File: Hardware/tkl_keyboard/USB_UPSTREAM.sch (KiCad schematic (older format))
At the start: 20 parts, among them J1 USB_C_Receptacle_USB2.0, U1 TCR2EF33, U2 SRV05-4

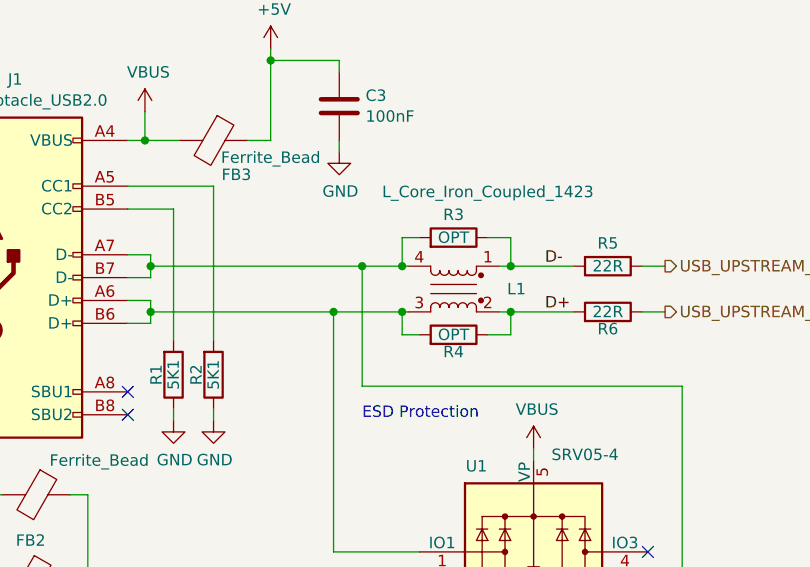
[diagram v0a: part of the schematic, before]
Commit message: Rows and columns routed to controller. Extended top board edge to fit OLED. Removed optional resistors around CMC.
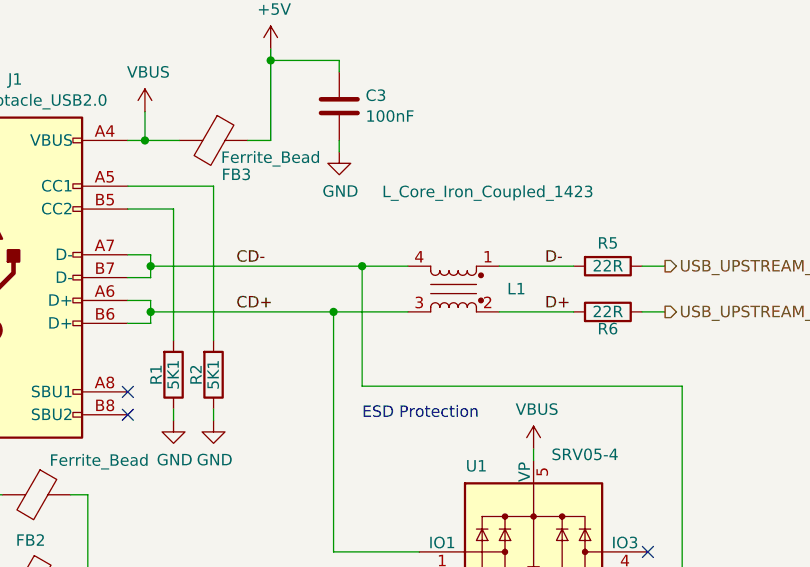
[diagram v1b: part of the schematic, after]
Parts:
- removed R5, R6: OPT, resistor_smd:R_0603_1608Metric, symbol Device:R
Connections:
- net CD+: now reaches J1.A6 (D+), J1.B6 (D+), L1.3, U2.1 (IO1)
- net CD-: now reaches J1.A7 (D-), J1.B7 (D-), L1.4, U2.6 (IO4)
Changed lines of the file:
@@
 	-1   0    0    -1
 $EndComp
-Wire Wire Line
-	5675 3775 5725 3775
-$Comp
-L Device:R R6
-U 1 1 60DDF643
-P 5475 4075
-AR Path="/6114D32E/60DDF643" Ref="R6"  Part="1"
-AR Path="/6247A5CE/60DDF643" Ref="R?"  Part="1"
-AR Path="/612340DE/60DDF643" Ref="R6"  Part="1"
-AR Path="/62F6B81F/60DDF643" Ref="R4"  Part="1"
-F 0 "R4" V 5400 4075 50  0000 C CNN
-F 1 "OPT" V 5475 4075 50  0000 C CNN
-F 2 "resistor_smd:R_0603_1608Metric" V 5405 4075 50  0001 C CNN
-F 3 "~" H 5475 4075 50  0001 C CNN
-	1    5475 4075
-	0    1    -1   0
-$EndComp
-$Comp
-L Device:R R5
-U 1 1 60DDFB5E
-P 5475 3650
-AR Path="/6114D32E/60DDFB5E" Ref="R5"  Part="1"
-AR Path="/6247A5CE/60DDFB5E" Ref="R?"  Part="1"
-AR Path="/612340DE/60DDFB5E" Ref="R5"  Part="1"
-AR Path="/62F6B81F/60DDFB5E" Ref="R3"  Part="1"
-F 0 "R3" V 5575 3650 50  0000 C CNN
-F 1 "OPT" V 5475 3650 50  0000 C CNN
-F 2 "resistor_smd:R_0603_1608Metric" V 5405 3650 50  0001 C CNN
-F 3 "~" H 5475 3650 50  0001 C CNN
-	1    5475 3650
-	0    1    -1   0
-$EndComp
-Wire Wire Line
-	5325 4075 5250 4075
-Wire Wire Line
-	5250 4075 5250 3975
-Wire Wire Line
-	5250 3975 5275 3975
-Wire Wire Line
-	5675 3975 5725 3975
-Wire Wire Line
-	5625 4075 5725 4075
-Wire Wire Line
-	5725 4075 5725 3975
-Connection ~ 5725 3975
-Wire Wire Line
-	5725 3775 5725 3650
-Wire Wire Line
-	5725 3650 5625 3650
-Connection ~ 5725 3775
-Wire Wire Line
-	5325 3650 5250 3650
-Wire Wire Line
-	5250 3650 5250 3775
-Wire Wire Line
-	5250 3775 5275 3775
 Text Notes 7450 4775 0    50   ~ 0
 5V to 3V3 LDO\n200mA
@@
 	2725 4675 2725 4775
 Connection ~ 2725 4775
-Wire Wire Line
-	5725 3775 6000 3775
-Wire Wire Line
-	5725 3975 6000 3975
 Text Label 5875 3775 0    50   ~ 0
 D-
@@
 Wire Wire Line
 	4150 3975 4950 3975
-Wire Wire Line
-	5250 3775 5075 3775
-Connection ~ 5250 3775
 Connection ~ 5075 3775
-Wire Wire Line
-	5250 3975 4950 3975
-Connection ~ 5250 3975
 Connection ~ 4950 3975
+Text Label 4525 3775 0    50   ~ 0
+CD-
+Text Label 4525 3975 0    50   ~ 0
+CD+
+Wire Wire Line
+	5075 3775 5275 3775
+Wire Wire Line
+	5675 3775 6000 3775
+Wire Wire Line
+	4950 3975 5275 3975
+Wire Wire Line
+	5675 3975 6000 3975
 $EndSCHEMATC

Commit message: Updating schematic
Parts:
- removed C16: 100nF, Capacitor_smd:C_0603_1608Metric, symbol Device:C
- removed C30: 1uF, Capacitor_smd:C_0603_1608Metric, symbol Device:C
- removed D1: LED, Diode_SMD:D_0603_1608Metric, symbol Device:LED
- removed R2: 330R, resistor_smd:R_0603_1608Metric, symbol Device:R
- removed U1: TCR2EF33, custom_footprint_library:TCR2EF33_SOT25, symbol custom_parts_library:TCR2EF33
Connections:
- net +5V renamed +5V0_USB
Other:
- note removed: "5V to 3V3 LDO\n200mA"
- note removed: "Power LED"

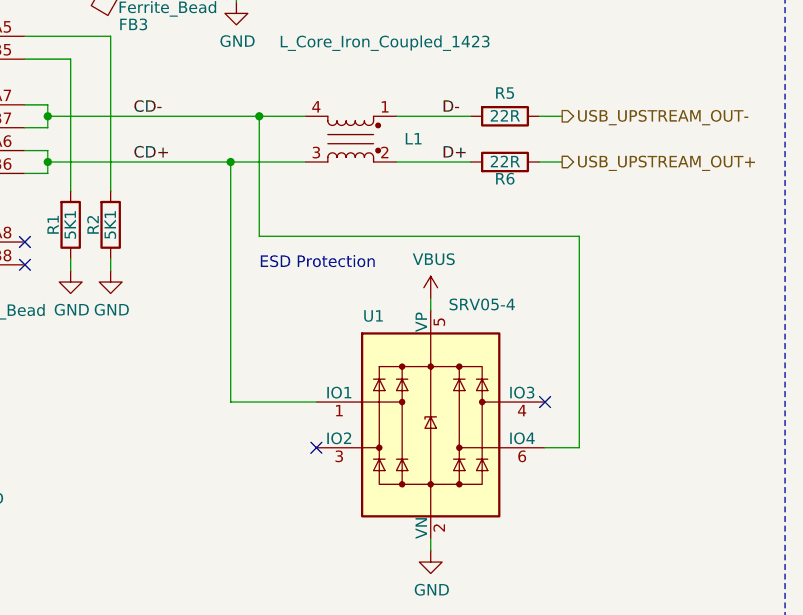
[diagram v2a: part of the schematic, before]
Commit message: First pass of routing done
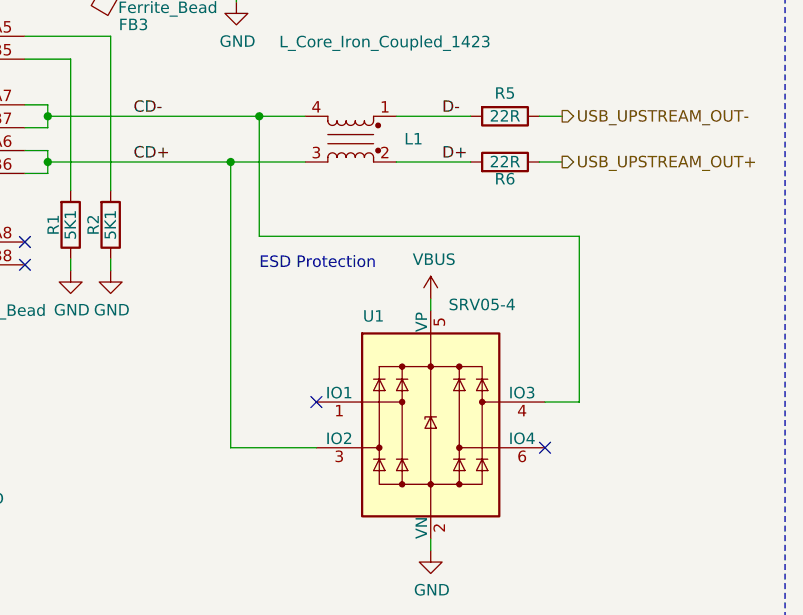
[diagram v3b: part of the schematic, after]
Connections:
- net CD+: now also U2.3 (IO2); no longer U2.1 (IO1)
- net CD-: now also U2.4 (IO3); no longer U2.6 (IO4)
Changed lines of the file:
@@
 Wire Wire Line
 	5075 3775 5075 4300
-NoConn ~ 6325 5025
+NoConn ~ 6325 5225
 Wire Wire Line
 	4975 2925 4975 2875
@@
 	5075 4300 6475 4300
 Wire Wire Line
-	6475 4300 6475 5225
-Wire Wire Line
-	6475 5225 6325 5225
-Wire Wire Line
-	5325 5025 4950 5025
-Wire Wire Line
-	4950 5025 4950 3975
-NoConn ~ 5325 5225
+	6475 4300 6475 5025
+NoConn ~ 5325 5025
 Wire Wire Line
 	3475 5150 3400 5150
@@
 	5250 2875 4975 2875
 Connection ~ 4975 2875
+Wire Wire Line
+	4950 5225 5325 5225
+Wire Wire Line
+	4950 3975 4950 5225
+Wire Wire Line
+	6325 5025 6475 5025
 $EndSCHEMATC

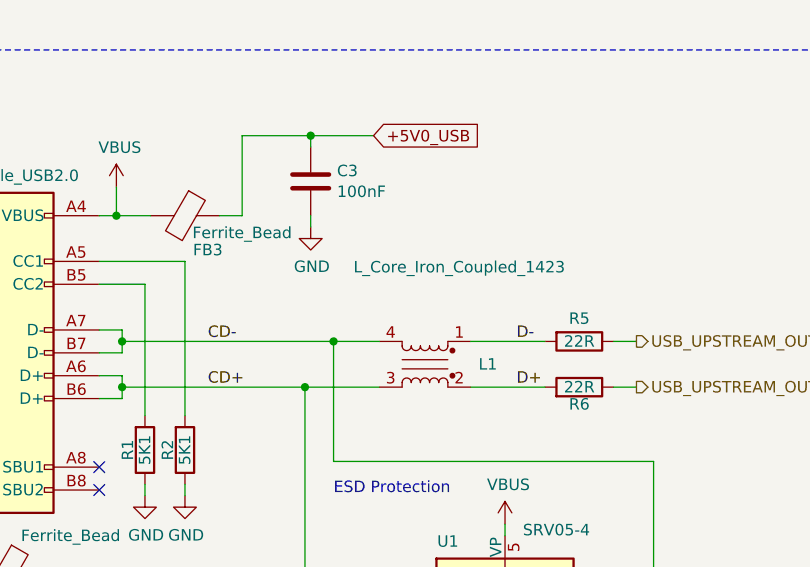
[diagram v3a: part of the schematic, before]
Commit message: Fixing USB circuit, adding data line resistors as per AN-5052
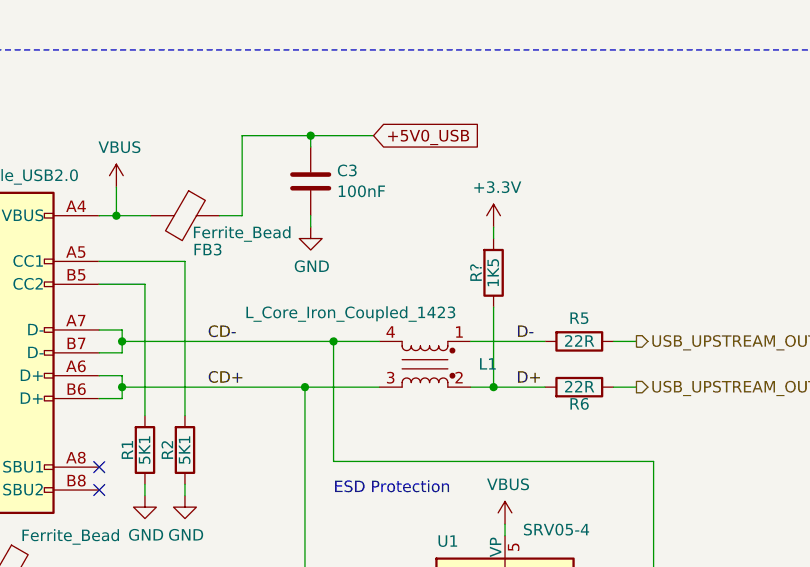
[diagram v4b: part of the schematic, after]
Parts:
- added R?: 1K5, resistor_smd:R_0603_1608Metric, symbol Device:R
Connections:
- net D+: now also R?.1
- new net +3V3: R?.2
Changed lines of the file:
@@
 AR Path="/62F6B81F/60DDC17D" Ref="L1"  Part="1"
 F 0 "L1" H 5200 3875 50  0000 C CNN
-F 1 "L_Core_Iron_Coupled_1423" H 5325 4300 50  0000 C CNN
+F 1 "L_Core_Iron_Coupled_1423" H 5800 4100 50  0000 C CNN
 F 2 "custom_footprint_library:SMM2012E" H 5475 3875 50  0001 C CNN
 F 3 "~" H 5475 3875 50  0001 C CNN
@@
 	4950 3975 5275 3975
 Wire Wire Line
-	5675 3975 6000 3975
+	5675 3975 5775 3975
 Text GLabel 5250 2875 2    50   Input ~ 0
 +5V0_USB
@@
 Wire Wire Line
 	6325 5025 6475 5025
+$Comp
+L Device:R R?
+U 1 1 614B1649
+P 5775 3475
+AR Path="/6114D32E/614B1649" Ref="R?"  Part="1"
+AR Path="/6247A5CE/614B1649" Ref="R?"  Part="1"
+AR Path="/612340DE/614B1649" Ref="R?"  Part="1"
+AR Path="/62F6B81F/614B1649" Ref="R?"  Part="1"
+F 0 "R?" V 5700 3475 50  0000 C CNN
+F 1 "1K5" V 5775 3475 50  0000 C CNN
+F 2 "resistor_smd:R_0603_1608Metric" V 5705 3475 50  0001 C CNN
+F 3 "~" H 5775 3475 50  0001 C CNN
+	1    5775 3475
+	1    0    0    1
+$EndComp
+Wire Wire Line
+	5775 3625 5775 3975
+Connection ~ 5775 3975
+Wire Wire Line
+	5775 3975 6000 3975
+$Comp
+L power:+3.3V #PWR?
+U 1 1 614B6C4F
+P 5775 3275
+AR Path="/6114D32E/614B6C4F" Ref="#PWR?"  Part="1"
+AR Path="/6247A5CE/614B6C4F" Ref="#PWR?"  Part="1"
+AR Path="/612340DE/614B6C4F" Ref="#PWR?"  Part="1"
+AR Path="/62F6B81F/614B6C4F" Ref="#PWR?"  Part="1"
+AR Path="/613390DE/614B6C4F" Ref="#PWR?"  Part="1"
+F 0 "#PWR?" H 5775 3125 50  0001 C CNN
+F 1 "+3.3V" H 5790 3448 50  0000 C CNN
+F 2 "" H 5775 3275 50  0001 C CNN
+F 3 "" H 5775 3275 50  0001 C CNN
+	1    5775 3275
+	1    0    0    -1
+$EndComp
+Wire Wire Line
+	5775 3325 5775 3275
 $EndSCHEMATC

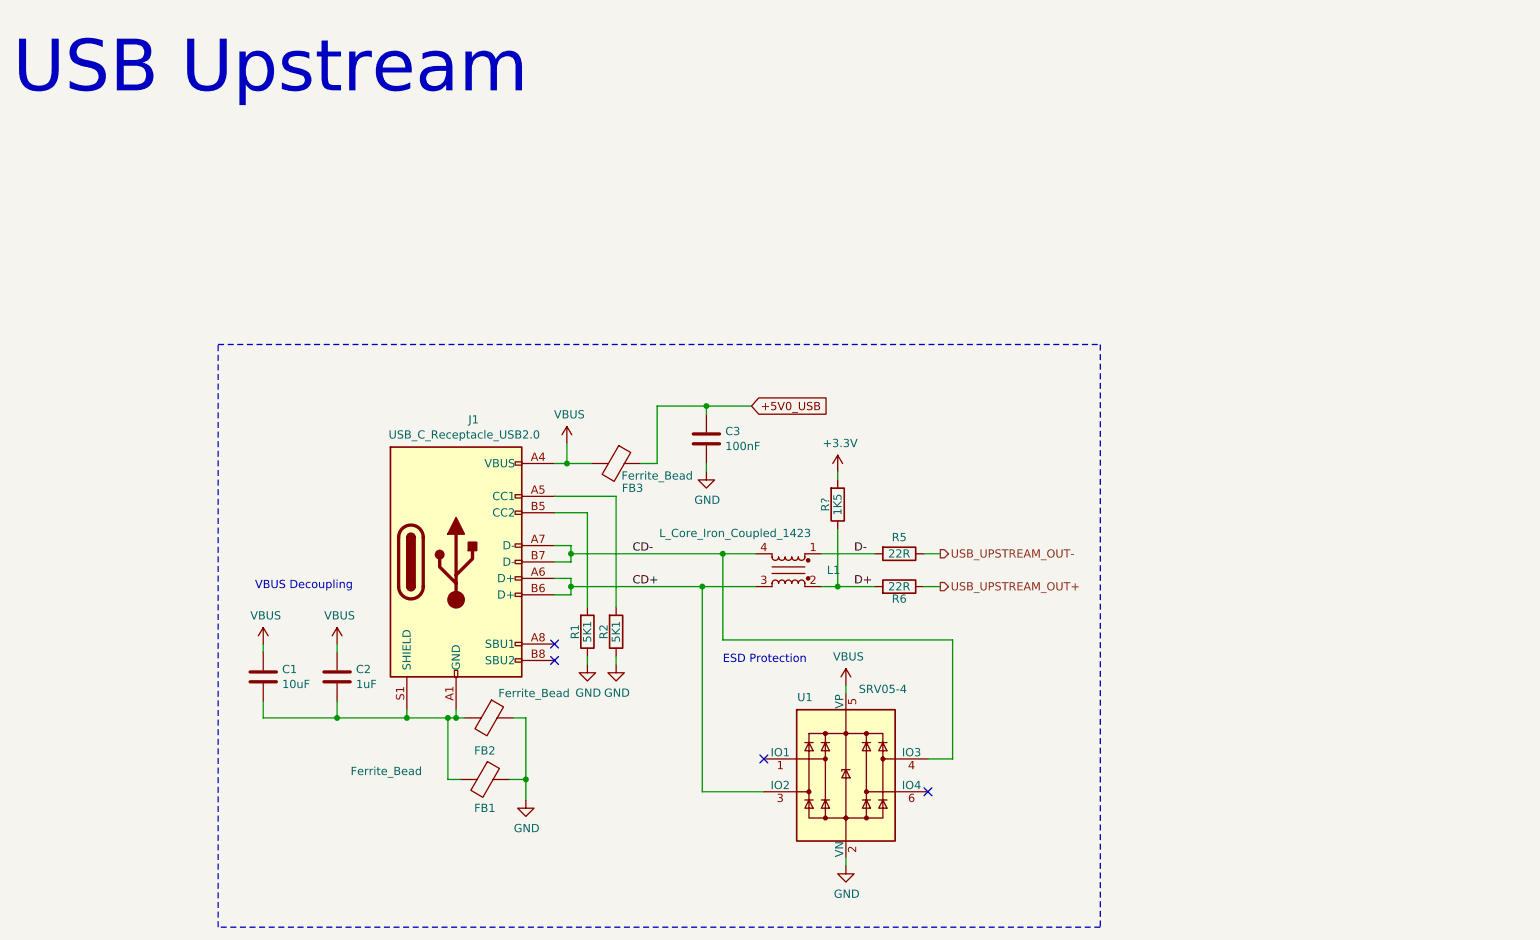
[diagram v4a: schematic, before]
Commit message: Tidying schematic
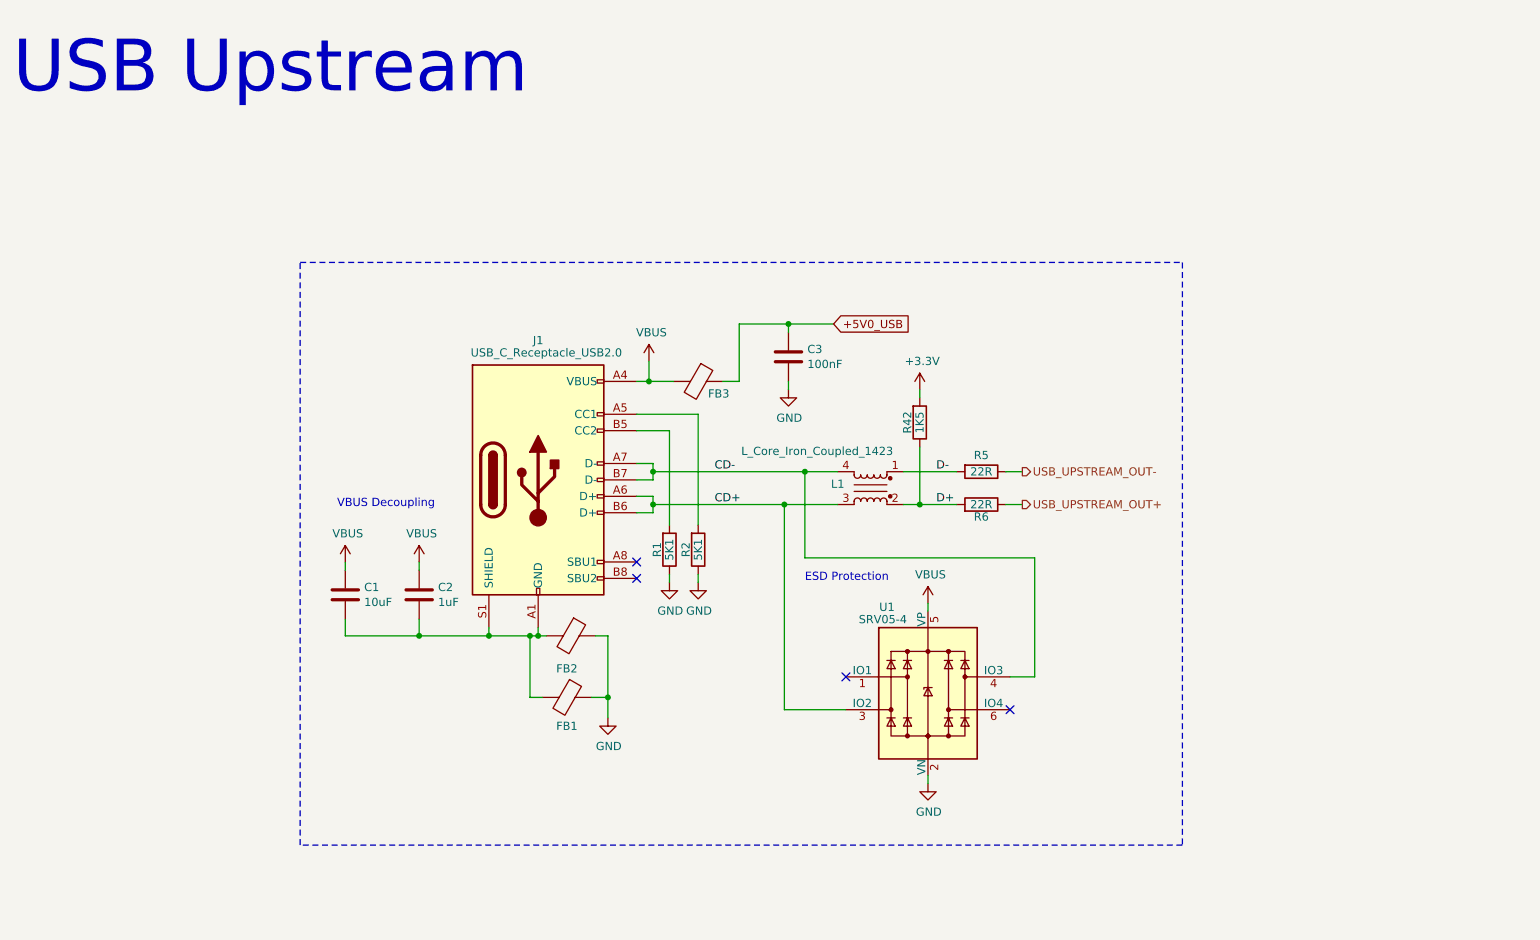
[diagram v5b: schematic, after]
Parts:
- gave numbers to parts that had none: 1
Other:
- moved on the sheet: C1, C2, C3, FB1, FB2, FB3, J1, L1, R1, R2, R42, R5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
